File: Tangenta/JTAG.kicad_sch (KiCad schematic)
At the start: 1 part, among them J28 Conn_02x05_Odd_Even

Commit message: Libraries exported from global to project.
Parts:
- J28: symbol Connector_Generic:Conn_02x05_Odd_Even -> CholaSymbolsPrjLib:Conn_02x05_Odd_Even
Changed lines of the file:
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@@
     )
   )
-  (symbol (lib_id "Connector_Generic:Conn_02x05_Odd_Even") (at 167.005 81.28 0) (mirror y) (unit 1)
+  (symbol (lib_id "CholaSymbolsPrjLib:Conn_02x05_Odd_Even") (at 167.005 81.28 0) (mirror y) (unit 1)
     (in_bom yes) (on_board yes) (dnp no)
     (property "Reference" "J28" (at 165.735 73.66 0)

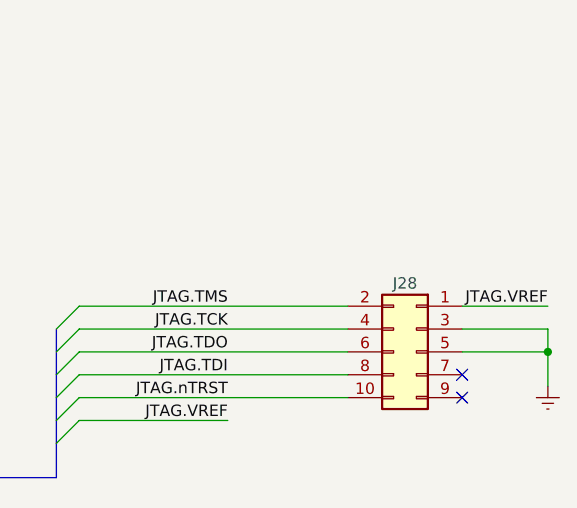
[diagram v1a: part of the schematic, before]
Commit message: Re-annotated. Ready for JLCPCB design verification.
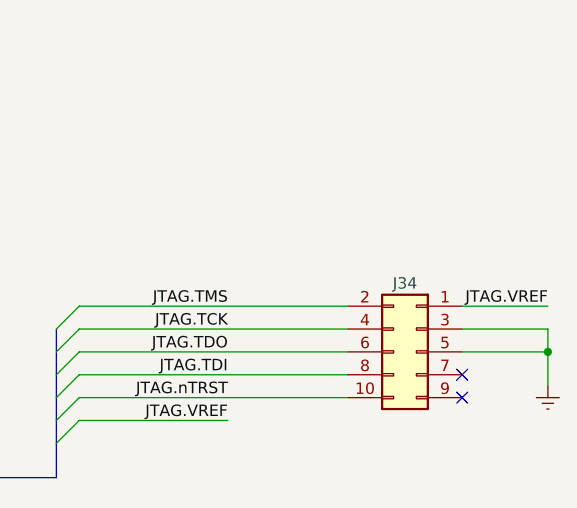
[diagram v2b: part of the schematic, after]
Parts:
- renumbered J28 to J34
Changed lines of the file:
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@@
         )
         (path "/358d1bcf-7599-4352-8c4d-baa18a5f09e6/9473c61f-5125-4990-b2e3-10b596e2b9c8"
-          (reference "#PWR0104") (unit 1)
+          (reference "#PWR0109") (unit 1)
         )
       )
@@
   (symbol (lib_id "CholaSymbolsPrjLib:Conn_02x05_Odd_Even") (at 167.005 81.28 0) (mirror y) (unit 1)
     (in_bom yes) (on_board yes) (dnp no)
-    (property "Reference" "J28" (at 165.735 73.66 0)
+    (property "Reference" "J34" (at 165.735 73.66 0)
       (effects (font (size 1.27 1.27)))
     )
@@
       (project "Tangenta"
         (path "/358d1bcf-7599-4352-8c4d-baa18a5f09e6/9473c61f-5125-4990-b2e3-10b596e2b9c8"
-          (reference "J28") (unit 1)
+          (reference "J34") (unit 1)
         )
       )
@@
         )
         (path "/358d1bcf-7599-4352-8c4d-baa18a5f09e6/9473c61f-5125-4990-b2e3-10b596e2b9c8"
-          (reference "#PWR0103") (unit 1)
+          (reference "#PWR0108") (unit 1)
         )
       )

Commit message: ...
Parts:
- J34: symbol CholaSymbolsPrjLib:Conn_02x05_Odd_Even -> LocalPrjLib:Conn_02x05_Odd_Even
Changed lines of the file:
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@@
     )
   )
-  (symbol (lib_id "CholaSymbolsPrjLib:Conn_02x05_Odd_Even") (at 167.005 81.28 0) (mirror y) (unit 1)
+  (symbol (lib_id "LocalPrjLib:Conn_02x05_Odd_Even") (at 167.005 81.28 0) (mirror y) (unit 1)
     (in_bom yes) (on_board yes) (dnp no)
     (property "Reference" "J34" (at 165.735 73.66 0)

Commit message: Fixes, new approach.
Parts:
- J34: symbol LocalPrjLib:Conn_02x05_Odd_Even -> LocalSymbolsPrjLib:Conn_02x05_Odd_Even
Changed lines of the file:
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@@
     )
   )
-  (symbol (lib_id "LocalPrjLib:Conn_02x05_Odd_Even") (at 167.005 81.28 0) (mirror y) (unit 1)
+  (symbol (lib_id "LocalSymbolsPrjLib:Conn_02x05_Odd_Even") (at 167.005 81.28 0) (mirror y) (unit 1)
     (in_bom yes) (on_board yes) (dnp no)
     (property "Reference" "J34" (at 165.735 73.66 0)
